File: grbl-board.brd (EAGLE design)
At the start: 100 x 85.1 mm, 29 parts, among them IC2 FT232RL, IC3 ADUM1250, IC4 LM2596S, X1 PN61729-S, X5 22-23-2021

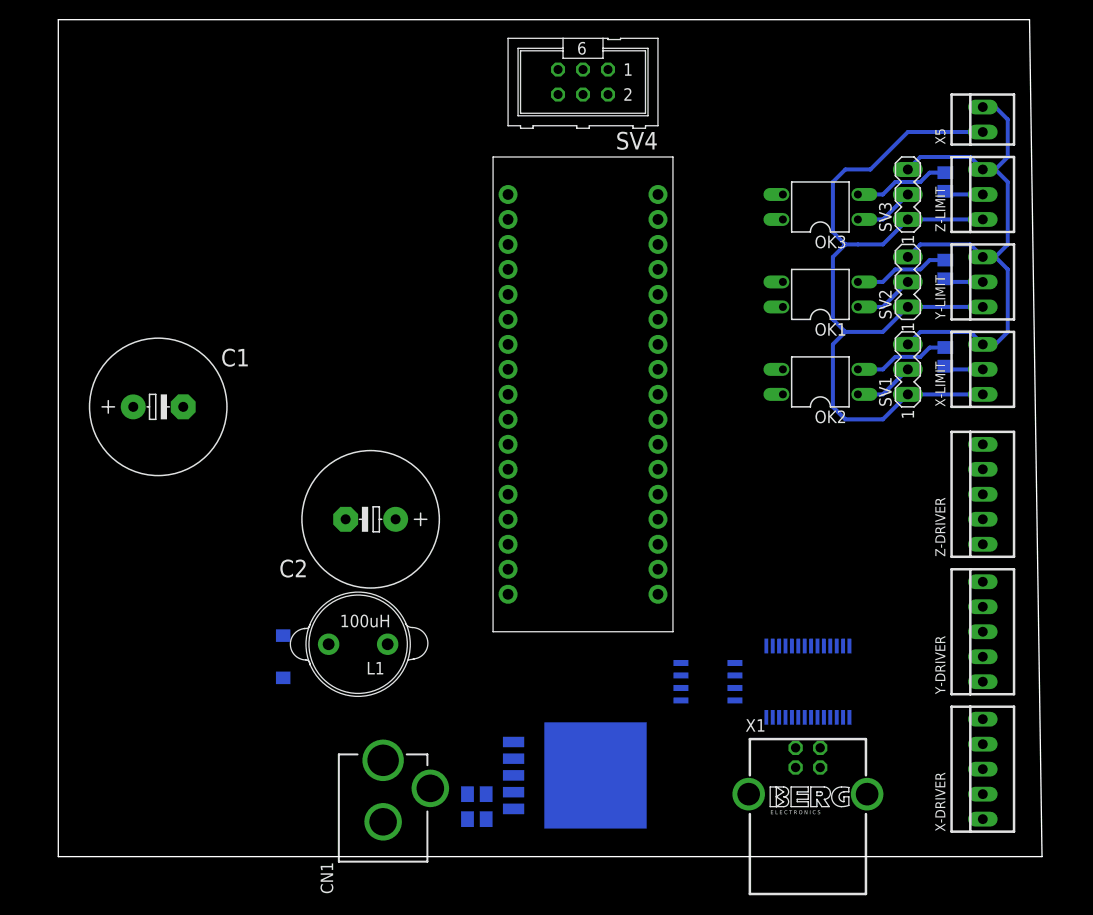
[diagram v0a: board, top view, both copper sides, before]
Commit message: del arduino
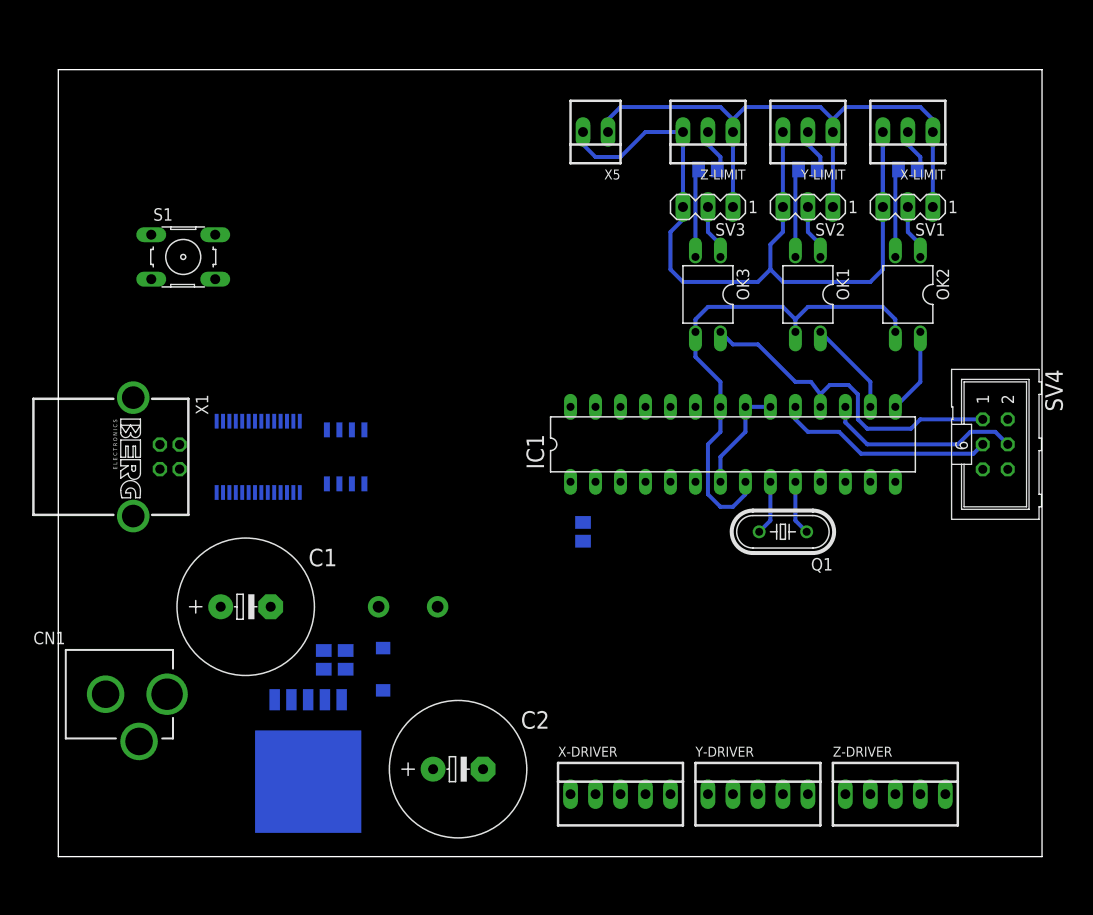
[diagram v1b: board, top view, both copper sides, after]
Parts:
- removed U$1: ARDUINOMICRO, adafruit:ARDUINOMICRO
- added IC1: MEGA8-P, atmel:DIL28-3
- added Q1: 16 MHz, crystal:HC49/S
- added R4: 10K, resistor:M0805
- added S1: (no value), switch-omron:B3F-10XX
- moved X1 76.7 mm to (7.62, 40.6), turned to 270 degrees
- moved IC2 60.4 mm to (20.3, 40.6)
- moved SV4 55.8 mm to (95.2, 41.9), turned to 270 degrees
- moved IC3 43.3 mm to (29.2, 40.6), turned to 180 degrees
- moved CN1 41.0 mm to (-2.54, 16.5), turned to 270 degrees
- moved X5 39.4 mm to (54.6, 73.7), turned to 180 degrees
- moved X-DRIVER 36.9 mm to (57.1, 6.35), turned to 0 degrees
- moved Z-DRIVER 31.8 mm to (85.1, 6.35), turned to 0 degrees
- moved Z-LIMIT 28.7 mm to (66.0, 73.7), turned to 180 degrees
- moved Y-DRIVER 28.2 mm to (71.1, 6.35), turned to 0 degrees
- moved C2 26.9 mm to (40.6, 8.89), turned to 0 degrees
- moved IC4 26.7 mm to (25.4, 10.2), turned to 180 degrees
- moved X-LIMIT 25.3 mm to (86.4, 73.7), turned to 180 degrees
- moved R3 24.2 mm to (66.0, 69.8), turned to 180 degrees
- moved Y-LIMIT 23.4 mm to (76.2, 73.7), turned to 180 degrees
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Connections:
- new net N$6: IC1.9, Q1.2
- new net N$7: IC1.10, Q1.1
- net (NOT_USED/RESERVED): now also IC1.27; no longer U$1.P$27
- net +5V: now also IC1.20, IC1.21, IC1.7, R4.2; no longer U$1.P$23, U$1.P$32
- net COOLANT_EN: now also IC1.26; no longer U$1.P$28
- net CYCLE_START/RESUME*: now also IC1.25; no longer U$1.P$29
- net FEED_HOLD*: now also IC1.24; no longer U$1.P$30
- net GND: now also IC1.22, IC1.8, S1.3; no longer U$1.P$12, U$1.P$21
- net PROBE*: now also IC1.28; no longer U$1.P$26
- net RESET: now also IC1.1, R4.1, S1.1; no longer U$1.P$13, U$1.P$22
- net RESET/ABORT*: now also IC1.23; no longer U$1.P$31
- net RXD: now also IC1.2; no longer U$1.P$14
- net SPINDLE-DIR: now also IC1.19; no longer U$1.P$34
- net SPINDLE-PWM: now also IC1.17; no longer U$1.P$2
- net STEPPER_EN: now also IC1.14; no longer U$1.P$5
- net TXD: now also IC1.3; no longer U$1.P$15
- net X-DIR: now also IC1.11; no longer U$1.P$8
- net X-LIMIT*: now also IC1.15; no longer U$1.P$4
- net X-STEP: now also IC1.4; no longer U$1.P$11
- net Y-DIR: now also IC1.12; no longer U$1.P$7
- net Y-LIMIT*: now also IC1.16; no longer U$1.P$3
- net Y-STEP: now also IC1.5; no longer U$1.P$10
- net Z-DIR: now also IC1.13; no longer U$1.P$6
- net Z-LIMIT*: now also IC1.18; no longer U$1.P$1
- net Z-STEP: now also IC1.6; no longer U$1.P$9
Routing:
- net GND: track 0.00 -> 50.5 mm
- net DGND: track 58.4 -> 94.9 mm
- net Z-LIMIT*: track 0.00 -> 34.8 mm
- net +24V: track 89.2 -> 64.1 mm
- net SPINDLE-DIR: track 0.00 -> 22.2 mm
- net SPINDLE-PWM: track 0.00 -> 20.1 mm
- net +5V: track 0.00 -> 11.2 mm
- net Y-LIMIT*: track 0.00 -> 9.72 mm
- net X-LIMIT*: track 0.00 -> 8.67 mm
- net N$6: track 0.00 -> 5.55 mm
- net N$7: track 0.00 -> 5.55 mm
- net N$5: track 9.81 -> 9.02 mm
- net N$15: track 9.81 -> 9.02 mm
- net N$14: track 9.81 -> 9.02 mm
- net N$9: track 3.94 -> 4.47 mm
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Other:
- board size 100 x 85.1 mm -> 100 x 80 mm

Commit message: add buttons
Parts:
- removed S1: (no value), switch-omron:B3F-10XX
- removed X5: 22-23-2021, con-molex:22-23-2021
- added 24V: 22-23-2021, con-molex:22-23-2021
- added FEED_HOLD, PROBE, RESET/ABORT, START/RESUME: 22-23-2031, con-molex:22-23-2031
- added OK4, OK5, OK6, OK7: PC814, optocoupler:DIL04
- added R10, R7, R8, R9: 1K, resistor:M0805
- added SV5, SV6, SV7, SV8: (no value), con-lstb:MA03-1
- moved CN1 22.9 mm to (-2.54, 39.4)
- moved IC2 17.8 mm to (20.3, 58.4)
- moved X1 17.8 mm to (7.62, 58.4)
- moved IC3 9.86 mm to (23.8, 48.9), turned to 0 degrees
- moved R3 8.01 mm to (70.5, 63.2), turned to 90 degrees
- moved R2 6.84 mm to (78.7, 63.5), turned to 90 degrees
- moved R1 6.38 mm to (87.0, 63.5), turned to 90 degrees
- moved OK2 2.84 mm to (83.8, 58.4)
- moved SV1 2.84 mm to (83.8, 67.3), turned to 0 degrees
- moved X-LIMIT 2.54 mm to (83.8, 73.7)
- moved OK3 1.80 mm to (67.3, 58.4)
- moved SV3 1.80 mm to (67.3, 67.3), turned to 0 degrees
- moved OK1 1.42 mm to (75.6, 58.4)
- moved SV2 1.42 mm to (75.6, 67.3), turned to 0 degrees
- moved Z-LIMIT 1.27 mm to (67.3, 73.7)
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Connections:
- removed net VDD1: IC3.1
- new net N$17: OK4.2, SV5.2
- new net N$20: OK4.1, R7.1
- new net N$21: OK5.2, SV6.2
- new net N$22: OK6.2, SV7.2
- new net N$23: OK7.2, SV8.2
- new net N$24: OK5.1, R8.1
- new net N$25: OK6.1, R9.1
- new net N$26: OK7.1, R10.1
- new net N$27: PROBE.1, R10.2
- new net N$28: R9.2, START/RESUME.1
- new net N$29: FEED_HOLD.1, R8.2
- new net N$30: R7.2, RESET/ABORT.1
- net +24V: now also 24V.1, FEED_HOLD.3, PROBE.3, RESET/ABORT.3, START/RESUME.3, SV5.1, SV6.1, SV7.1, SV8.1, X-LIMIT.3, Y-LIMIT.3, Z-LIMIT.3; no longer X-LIMIT.1, X5.1, Y-LIMIT.1, Z-LIMIT.1
- net +5V: now also IC3.1
- net CYCLE_START/RESUME*: now also OK6.4
- net DGND: now also 24V.2, FEED_HOLD.2, PROBE.2, RESET/ABORT.2, START/RESUME.2, SV5.3, SV6.3, SV7.3, SV8.3, X-LIMIT.2, Y-LIMIT.2, Z-LIMIT.2; no longer X-LIMIT.3, X5.2, Y-LIMIT.3, Z-LIMIT.3
- net FEED_HOLD*: now also OK5.4
- net GND: now also OK4.3, OK5.3, OK6.3, OK7.3; no longer S1.3
- net N$10: now also R3.1; no longer SV3.2
- net N$11: now also OK3.2, SV3.2; no longer OK1.1, SV2.2
- net N$12: now also OK2.2; no longer OK2.1
- net N$13: now also X-LIMIT.1; no longer X-LIMIT.2
- net N$14: now also OK1.2, SV2.2; no longer OK3.2, R3.1
- net N$15: now also OK1.1; no longer OK1.2
- net N$5: now also OK2.1; no longer OK2.2
- net N$8: now also Y-LIMIT.1; no longer Y-LIMIT.2
- net N$9: now also Z-LIMIT.1; no longer Z-LIMIT.2
- net PROBE*: now also OK7.4
- net RESET: no longer S1.1
- net RESET/ABORT*: now also OK4.4
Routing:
- net +24V: track 64.1 -> 158.9 mm
- net GNDA: track 0.00 -> 53.6 mm
- net DGND: track 94.9 -> 134.7 mm
- net Z-LIMIT*: track 34.8 -> 0.00 mm
- net SPINDLE-DIR: track 22.2 -> 0.00 mm
- net SPINDLE-PWM: track 20.1 -> 0.00 mm
- net +5V: track 11.2 -> 0.00 mm
- net N$28: track 0.00 -> 10.6 mm
- net N$30: track 0.00 -> 10.6 mm
- net N$29: track 0.00 -> 10.6 mm
- net N$27: track 0.00 -> 10.6 mm
- net GND: track 50.5 -> 60.3 mm
- net Y-LIMIT*: track 9.72 -> 0.00 mm
- net X-LIMIT*: track 8.67 -> 0.00 mm
- net N$4: track 0.00 -> 8.13 mm
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
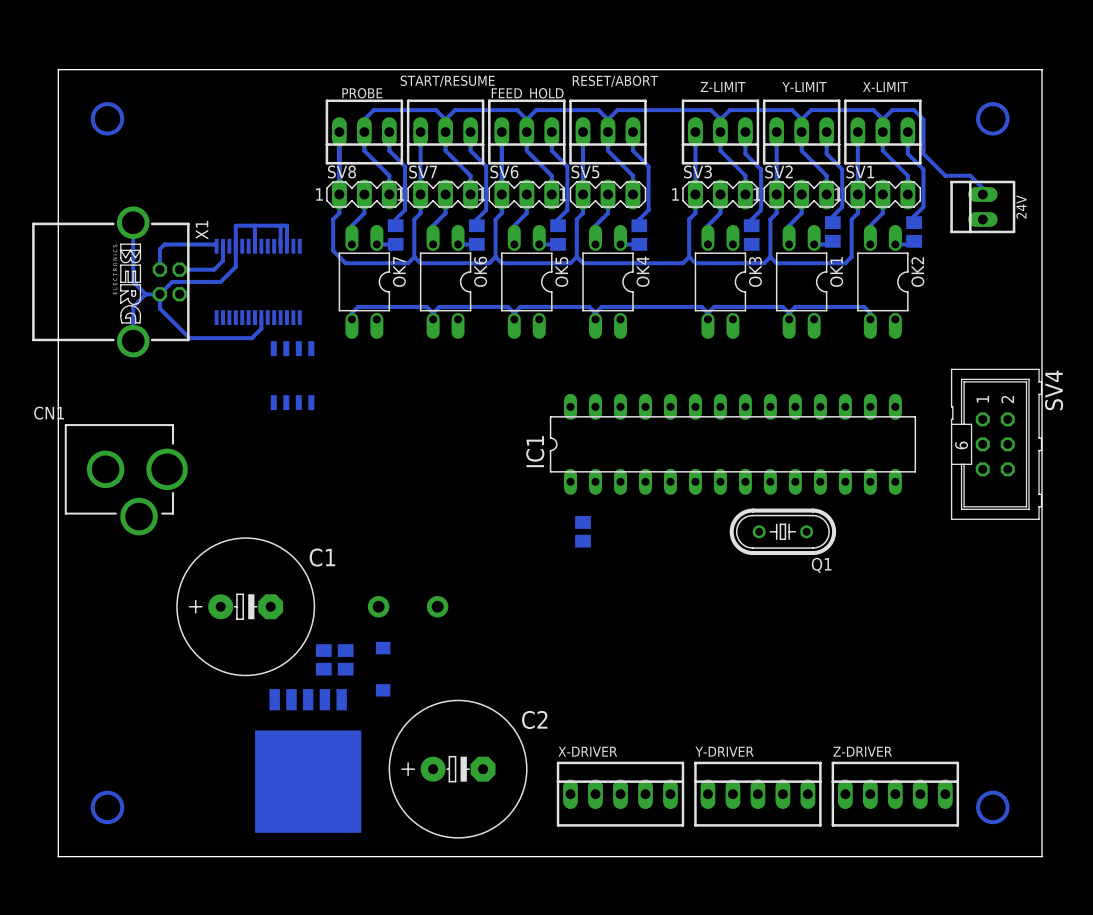
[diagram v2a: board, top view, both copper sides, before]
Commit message: add spindle
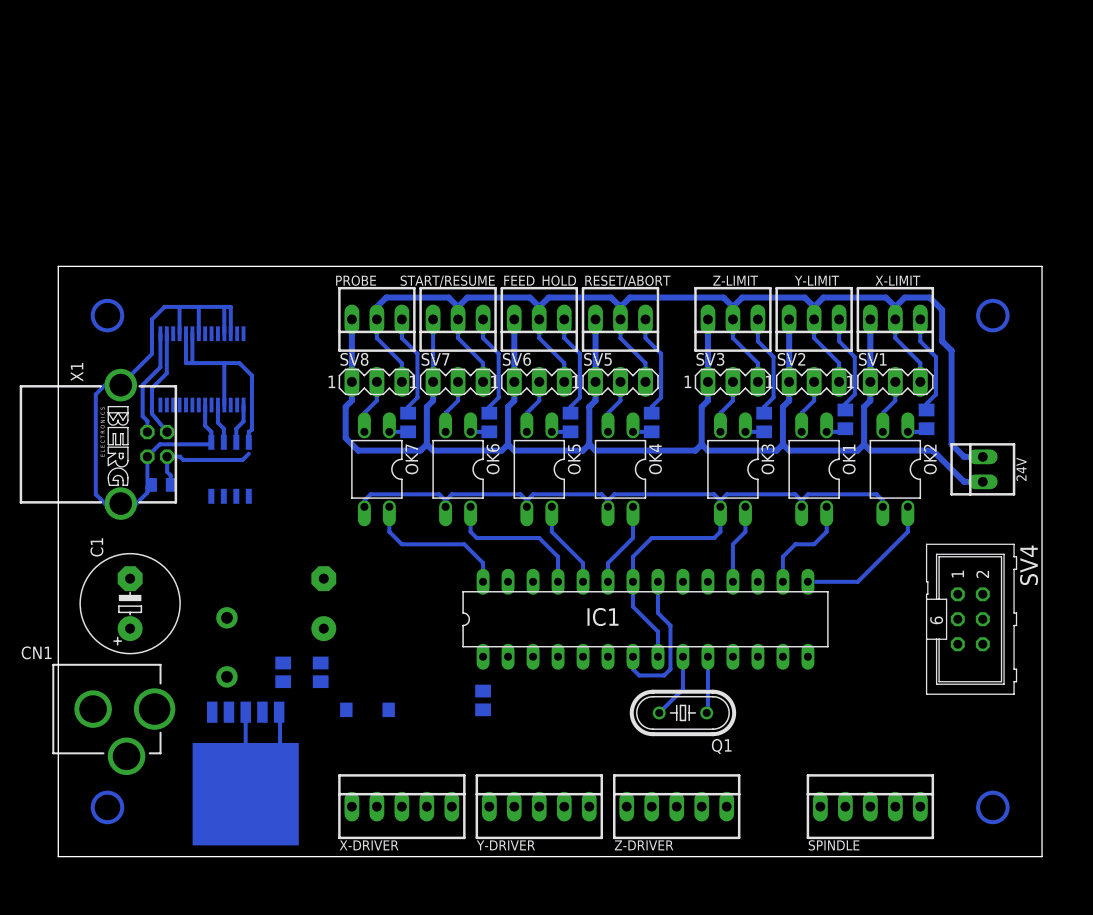
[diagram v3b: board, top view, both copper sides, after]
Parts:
- added C3: (no value), adafruit:C0805K
- added SPINDLE: 22-23-2051, con-molex:22-23-2051
- C1, C2: device adafruit:E5-13 -> adafruit:E5-10,5
- IC1: value MEGA8-P -> MEGA328-P
- IC3: value ADUM1250 -> ADuM1201AR
- moved 24V 26.7 mm to (94.0, 39.4)
- moved CN1 24.4 mm to (-3.81, 15.0)
- moved X-DRIVER 22.3 mm to (34.9, 5.08)
- moved Y-DRIVER 22.3 mm to (48.9, 5.08)
- moved Z-DRIVER 22.3 mm to (62.9, 5.08)
- moved C2 21.7 mm to (27.0, 25.7), flipped to the bottom, turned to 90 degrees
- moved Q1 21.0 mm to (63.5, 14.6)
- moved R4 19.9 mm to (43.2, 15.9)
- moved IC1 19.9 mm to (59.7, 24.1)
- moved OK1 19.1 mm to (76.8, 39.4)
- moved OK2 19.1 mm to (85.1, 39.4)
- moved OK3 19.1 mm to (68.6, 39.4)
- moved OK4 19.1 mm to (57.1, 39.4)
- moved OK5 19.1 mm to (48.9, 39.4)
- moved OK6 19.1 mm to (40.6, 39.4)
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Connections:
- removed net GND2: IC3.5
- net +5V: now also SPINDLE.1
- net COOLANT_EN: now also SPINDLE.5
- net GND: now also SPINDLE.2
- net GNDA: now also C3.2, IC3.5
- net SPINDLE-DIR: now also SPINDLE.4
- net SPINDLE-PWM: now also SPINDLE.3
- net VDD2: now also C3.1
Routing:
- net GND: track 60.3 -> 99.6 mm
- net VDD2: track 0.00 -> 36.2 mm
- net PROBE*: track 0.00 -> 15.3 mm
- net CYCLE_START/RESUME*: track 0.00 -> 15.0 mm
- net +5V: track 0.00 -> 15.0 mm
- net X-LIMIT*: track 0.00 -> 14.8 mm
- net +24V: track 158.9 -> 172.6 mm
- net Y-LIMIT*: track 0.00 -> 10.6 mm
- net FEED_HOLD*: track 0.00 -> 8.94 mm
- net RESET/ABORT*: track 0.00 -> 8.67 mm
- net GNDA: track 53.6 -> 62.0 mm
- net Z-LIMIT*: track 0.00 -> 8.15 mm
- net DGND: track 134.7 -> 141.6 mm
- net N$6: track 0.00 -> 6.71 mm
- net N$7: track 0.00 -> 5.77 mm
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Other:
- board size 100 x 80 mm -> 100 x 60 mm

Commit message: route power supply
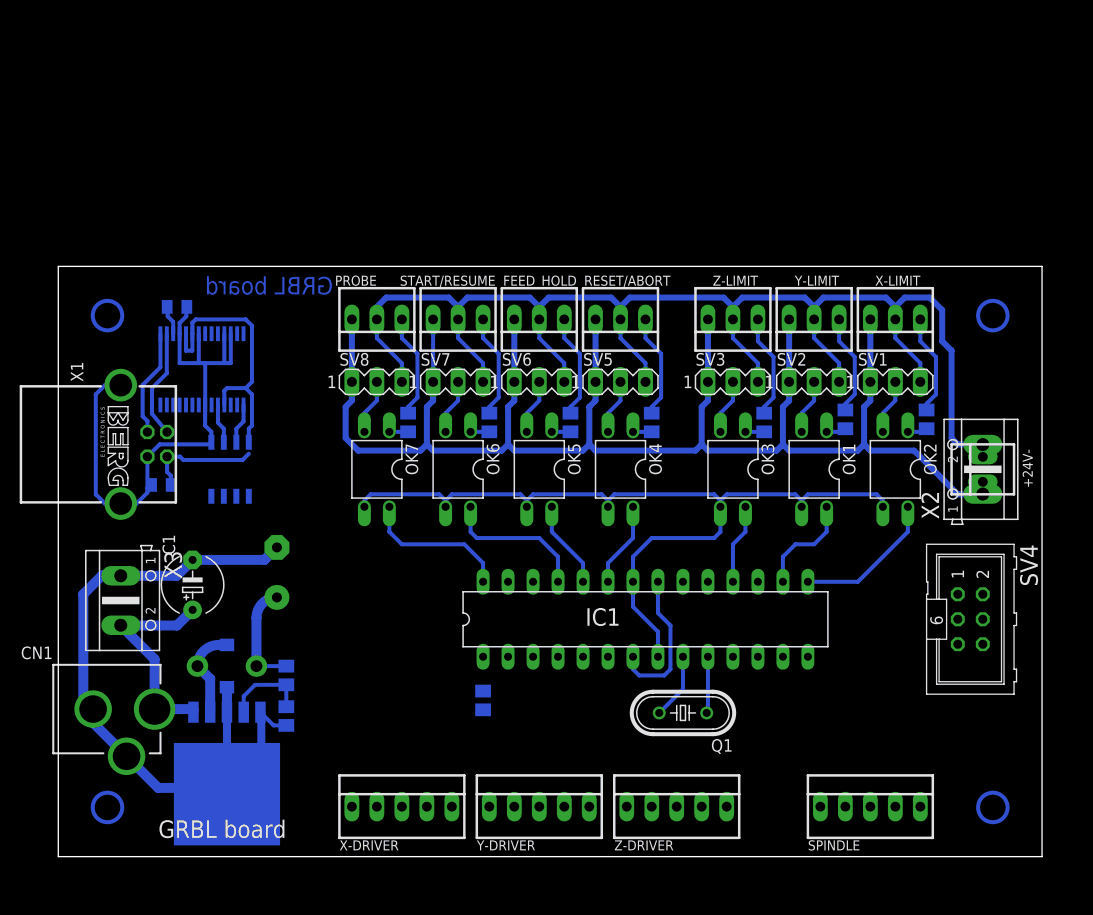
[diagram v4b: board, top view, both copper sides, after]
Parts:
- added C4: (no value), adafruit:C0805K
- added X2, X3: (no value), con-ptr500:AK500/2
- C1: device adafruit:E5-10,5 -> adafruit:E5-6
- moved D1 15.0 mm to (17.1, 19.4), turned to 90 degrees
- moved C1 6.63 mm to (13.7, 27.6)
- moved C2 5.72 mm to (22.2, 28.9)
- moved R5 4.46 mm to (23.2, 14.3)
- moved R6 3.51 mm to (23.2, 18.4)
- moved IC4 1.91 mm to (17.1, 8.89)
- moved L1 1.91 mm to (17.1, 19.4), turned to 0 degrees
- renumbered 24V to +24V-
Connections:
- new net N$31: C4.1, IC2.17
- net +24V: now also X2.1
- net DGND: now also X2.2
- net GND: now also X3.1
- net GNDA: now also C4.2
- net N$19: now also X3.2
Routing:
- net GND: track 99.6 -> 164.1 mm
- net N$19: track 0.00 -> 22.2 mm
- net +5V: track 15.0 -> 25.9 mm
- net N$16: track 0.00 -> 9.23 mm
- net N$18: track 0.00 -> 8.66 mm
- net VDD2: track 36.2 -> 39.7 mm
- net N$31: track 0.00 -> 2.98 mm
- net GNDA: track 62.0 -> 59.0 mm
- net DGND: track 141.6 -> 140.7 mm
- net +24V: track 172.6 -> 173.1 mm
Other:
- board text added: "GRBL board"

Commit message: route round lines refactor
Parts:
- removed X3: (no value), con-ptr500:AK500/2
- moved R4 9.34 mm to (48.6, 23.5), turned to 180 degrees
- moved C2 9.21 mm to (13.0, 29.2), turned to 0 degrees
- moved C1 8.67 mm to (6.03, 23.5), turned to 180 degrees
- moved C3 0.71 mm to (10.2, 38.4)
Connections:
- net GND: no longer X3.1
- net N$19: no longer X3.2
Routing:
- net +5V: track 25.9 -> 167.9 mm
- net X-DIR: track 0.00 -> 73.7 mm
- net GND: track 164.1 -> 225.9 mm
- net TXD: track 0.00 -> 42.1 mm
- net Y-DIR: track 0.00 -> 41.6 mm
- net STEPPER_EN: track 0.00 -> 39.6 mm
- net RXD: track 0.00 -> 35.1 mm
- net X-STEP: track 0.00 -> 28.1 mm
- net Z-STEP: track 0.00 -> 25.4 mm
- net Z-DIR: track 0.00 -> 18.7 mm
- net Y-STEP: track 0.00 -> 17.1 mm
- net +24V: track 173.1 -> 158.2 mm
- net RESET: track 0.00 -> 10.8 mm
- net N$19: track 22.2 -> 15.1 mm
- net N$4: track 10.9 -> 12.2 mm
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
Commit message: rounded commit
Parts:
- moved SV4 2.62 mm to (93.3, 21.6)
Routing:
- net SPINDLE-DIR: track 0.00 -> 29.5 mm
- net GND: track 225.9 -> 254.9 mm
- net SPINDLE-PWM: track 0.00 -> 28.0 mm
- net Z-LIMIT*: track 8.15 -> 33.5 mm
- net N$14: track 5.61 -> 0.00 mm
- net Y-DIR: track 41.6 -> 36.1 mm
- net X-DIR: track 73.7 -> 70.1 mm
- net N$8: track 10.3 -> 9.31 mm
- net N$9: track 10.6 -> 9.63 mm
- net Y-LIMIT*: track 10.2 -> 9.32 mm
- net DGND: track 140.6 -> 139.8 mm
- net N$13: track 10.3 -> 9.61 mm
- net +5V: track 167.9 -> 167.4 mm
- net RESET/ABORT*: track 8.67 -> 8.16 mm

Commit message: refactor
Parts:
- removed X-DRIVER, Y-DRIVER, Z-DRIVER: 22-23-2051, con-molex:22-23-2051
- added X, Y, Z: 22-23-2041, con-molex:22-23-2041
- SPINDLE: value 22-23-2051 -> 22-23-2041; device con-molex:22-23-2051 -> con-molex:22-23-2041
- moved R4 8.58 mm to (43.2, 16.8), turned to 270 degrees
- moved SPINDLE 1.42 mm to (83.8, 4.45)
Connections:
- net +5V: no longer SPINDLE.1, SV4.2, X-DRIVER.1, Y-DRIVER.1, Z-DRIVER.1
- net COOLANT_EN: now also SPINDLE.1; no longer SPINDLE.5
- net GND: now also SPINDLE.4, X.4, Y.4, Z.4; no longer SPINDLE.2, X-DRIVER.2, Y-DRIVER.2, Z-DRIVER.2
- net SPINDLE-DIR: now also SPINDLE.2; no longer SPINDLE.4
- net STEPPER_EN: now also X.3, Y.3, Z.3; no longer X-DRIVER.5, Y-DRIVER.5, Z-DRIVER.5
- net X-DIR: now also IC1.5, X.2; no longer IC1.11, X-DRIVER.4
- net X-STEP: now also X.1; no longer X-DRIVER.3
- net Y-DIR: now also IC1.11, Y.2; no longer IC1.12, Y-DRIVER.4
- net Y-STEP: now also IC1.6, Y.1; no longer IC1.5, Y-DRIVER.3
- net Z-DIR: now also Z.2; no longer Z-DRIVER.4
- net Z-STEP: now also IC1.12, Z.1; no longer IC1.6, Z-DRIVER.3
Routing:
- net +5V: track 167.4 -> 112.2 mm
- net X-DIR: track 70.1 -> 27.2 mm
- net STEPPER_EN: track 39.6 -> 65.1 mm
- net SPINDLE-PWM: track 28.0 -> 50.5 mm
- net SPINDLE-DIR: track 29.5 -> 49.4 mm
- net Z-DIR: track 19.0 -> 28.9 mm
- net RESET: track 10.8 -> 2.54 mm
- net GND: track 254.9 -> 262.8 mm
- net N$14: track 0.00 -> 5.38 mm
- net Y-STEP: track 17.1 -> 21.8 mm
- net Z-STEP: track 25.4 -> 28.0 mm
- net Y-DIR: track 36.1 -> 33.6 mm
- net DGND: track 139.8 -> 138.6 mm
- net N$30: track 10.6 -> 9.63 mm
- net N$27: track 10.6 -> 9.63 mm
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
